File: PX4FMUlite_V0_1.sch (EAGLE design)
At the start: 168 parts, among them J201 DF13C-6P-1.25V, J202 DF13C-6P-1.25V, J203 DF13C-6P-1.25V, J204 DF13C-6P-1.25V, J301 47346-0001, J302 DF13C-4P-1.25V, J401 DF13C-4P-1.25V, J403 DF13C-7P-1.25V, J404 DF13C-5P-1.25V, J405 DF13C-4P-1.25V, J601 DF13C-6P-1.25V, J702 DF13C-3P-1.25V, J801 JST-ZH-3, M3_MOUNT1101 MOUNT-HOLE3.1MM, M3_MOUNT1102 MOUNT-HOLE3.1MM, M3_MOUNT1103 MOUNT-HOLE3.1MM, M3_MOUNT1104 MOUNT-HOLE3.1MM, U101 STM32F4X7VX, U102 FM25V01, U301 2908-05WB-MG, U401 MAX3051, U502 L3GD20H, U701 TCA62724FMG, U703 LRTB GFTG-T7AW-1+V7A7-29+R5T9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, U903 74LVC2G240, X101 3.2x2.5 mm / 24 MHz / 15 ppm

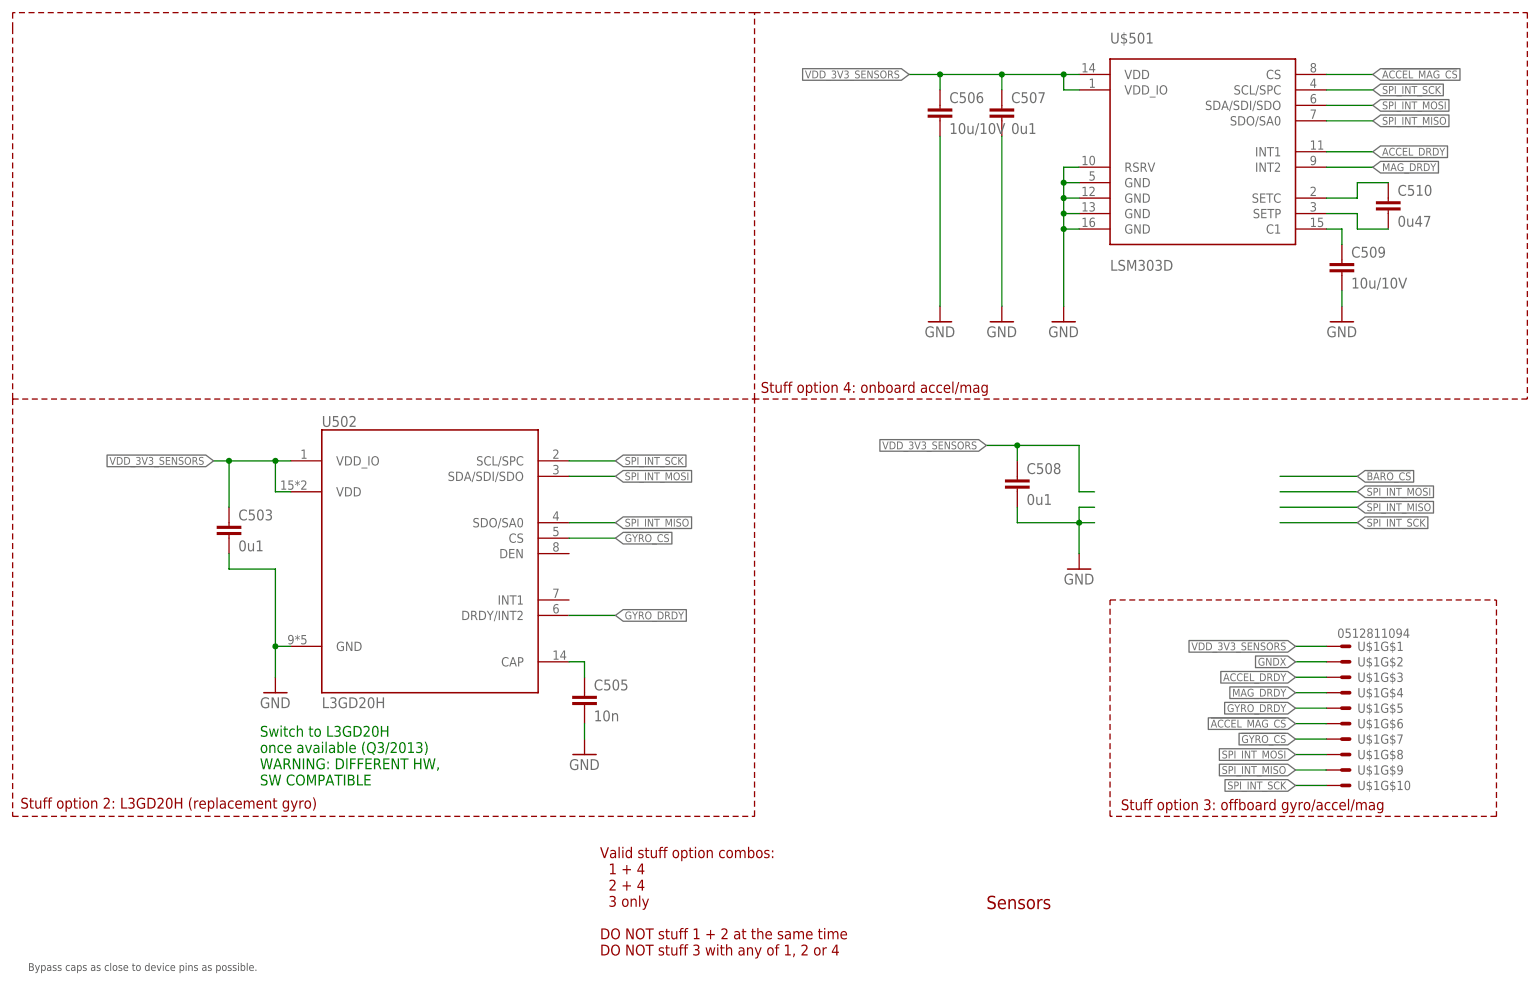
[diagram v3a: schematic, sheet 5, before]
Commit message: Change to MPU6000 (sparkfun - needs changing),  Removed DF13 powerbrick conn
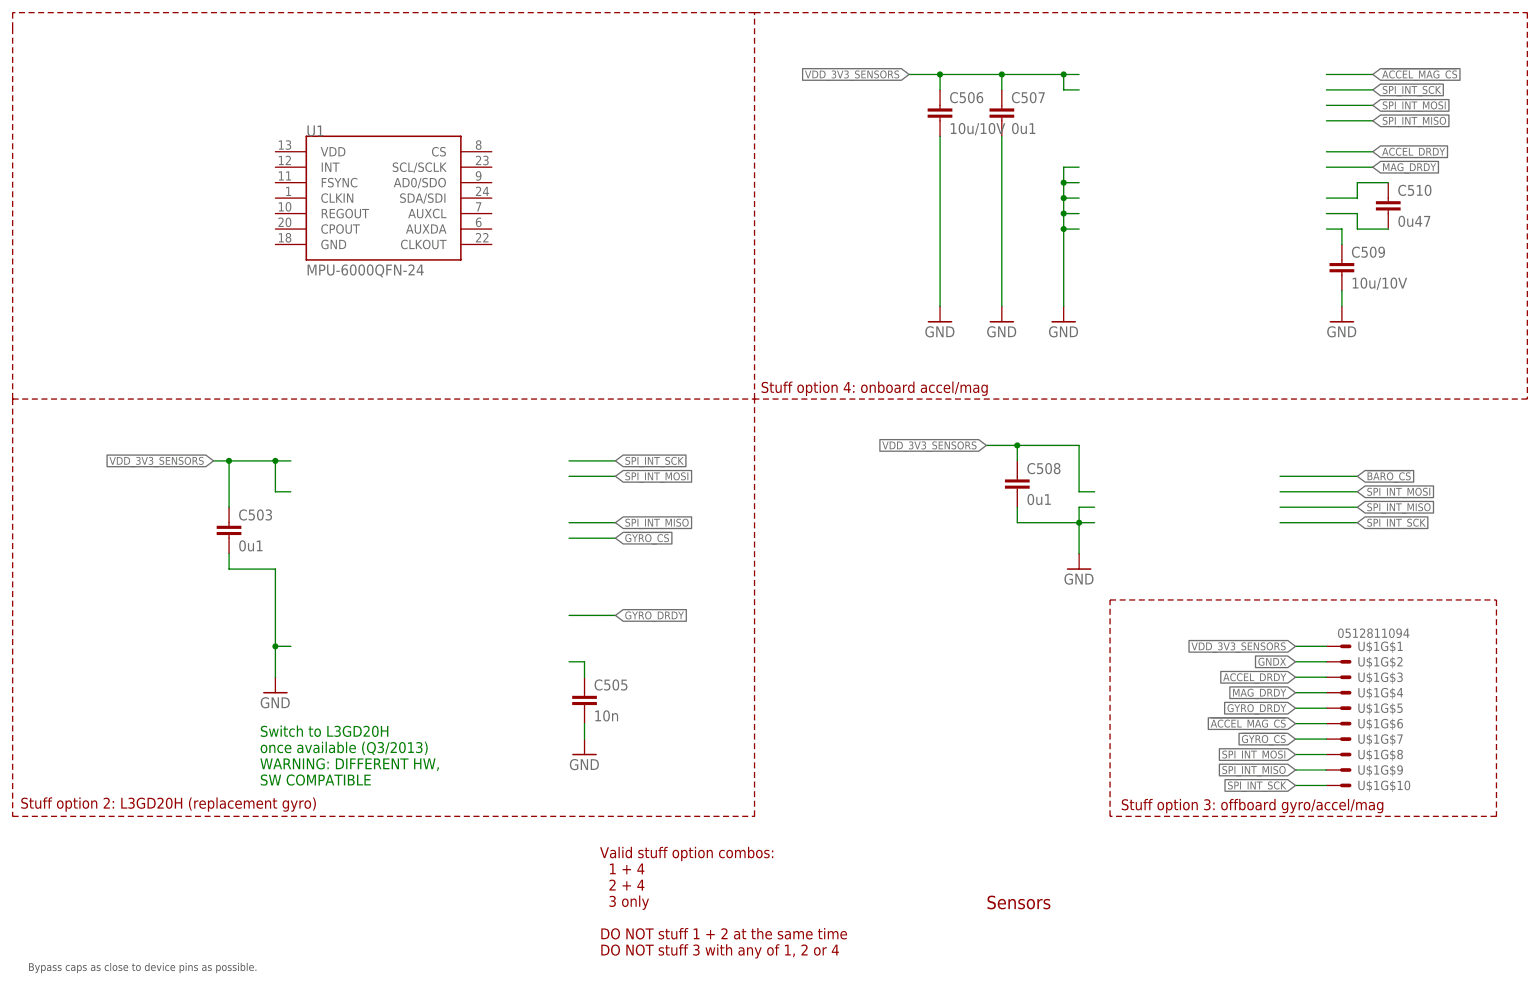
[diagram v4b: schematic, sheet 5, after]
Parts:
- removed D1001: PMEG2005CT, pixhawk2:PMEG2005CT
- removed F2: 0ZCA0035FF2G, pixhawk2:PTCSMD
- removed J601: DF13C-6P-1.25V, con-hirose-df13:DF13-6P-1.25V
- removed R1001: 100K, pixhawk2:RESISTOR0402-RES
- removed U$1001: BQ24313, pixhawk2:BQ24313
- removed U$501: LSM303D, pixhawk2:LSM303D
- removed U502: L3GD20H, pixhawk2:L3GD20H
- added U1: MPU-6000QFN-24, SparkFun-Sensors:MPU-6000QFN-24
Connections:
- net FMU-CH6 renamed FMU-CH8
- removed net BATT_CURRENT_SENS_PROT: J601.3, L601.P$1
- removed net IO-!VDD_SERVO_IN_FAULT: U$1001.!FAULT
- removed net IO-VDD_5V5: C1001.1, D1001.CC, LED702.A, LED703.A, LED705.A, U$1002.EN2, U$1002.VIN
- removed net N$20: R1001.2, U$1001.ILIM
- removed net N$4: D1001.A2, U$1001.OUT
- removed net N$46: D1001.A1, F2.2
- new net FMU-VDD_5V: C1001.1, LED702.A, LED703.A, LED705.A, U$1002.EN2, U$1002.VIN
- new net N$18: L1G$8.P$1
- new net N$21: L601.P$1
- net !ACCEL_MAG_CS: no longer U$501.CS
- net !GYRO_CS: no longer U502.CS
- net ACCEL_DRDY: no longer U$501.INT1
- net BATT_VOLTAGE_SENS_PROT: no longer J601.4
- net GNDX: no longer J601.5, J601.6, R1001.1, U$1001.!CE, U$1001.VBAT, U$1001.VSS, U$501.GND@1, U$501.GND@2, U$501.GND@3, U$501.GND@4, U$501.RSRV, U502.GND
- net GYRO_DRDY: no longer U502.DRDY/INT2
- net MAG_DRDY: no longer U$501.INT2
- net N$10: no longer U$501.SETC
- net N$17: no longer U$501.SETP
- net N$30: no longer U502.CAP
- net N$6: no longer U$501.C1
- net SPI_INT_MISO: no longer U$501.SDO/SA0, U502.SDO/SA0
- net SPI_INT_MOSI: no longer U$501.SDA/SDI/SDO, U502.SDA/SDI/SDO
- net SPI_INT_SCK: no longer U$501.SCL/SPC, U502.SCL/SPC
- net VDD_3V3_SENSORS: no longer U$501.VDD, U$501.VDD_IO, U502.VDD, U502.VDD_IO
- net VDD_5V_BRICK: no longer J601.1, J601.2
- net VDD_5V_IN: no longer F2.1
- net VDD_SERVO_IN: no longer U$1001.IN
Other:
- note removed: "Current limit = 25 / Rilim (current in A, R in kOhms) 100K = 250mA"
- note removed: "Dual supply from servo rail and FMU 5V rail"
- note removed: "Output voltage limited to 5.5V for input voltages up to 10.5V; output switches off at higher input voltages."
